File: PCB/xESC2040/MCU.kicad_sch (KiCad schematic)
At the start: 20 parts, among them J6 Conn_01x02, U2 RP2040, U3 W25Q128JVP, Y1 Crystal_GND24

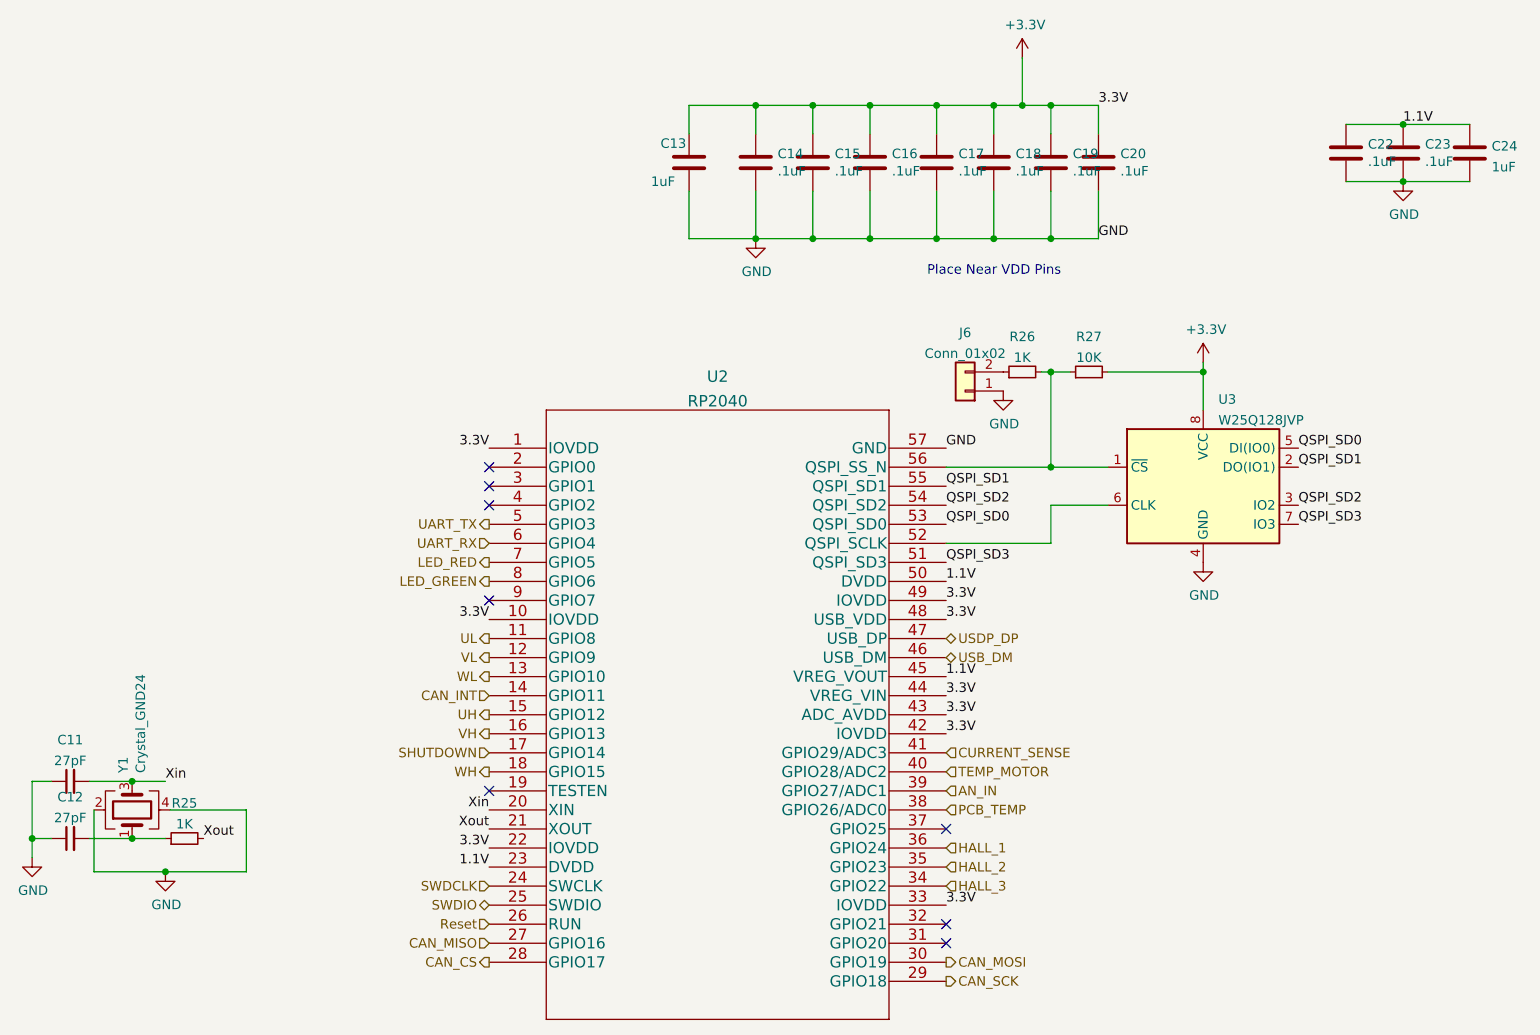
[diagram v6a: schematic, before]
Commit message: Merge J5 and J1 into one connector - no pinout changes or connector move
With J5 gone had kicad redo  reference designators - hope that's ok
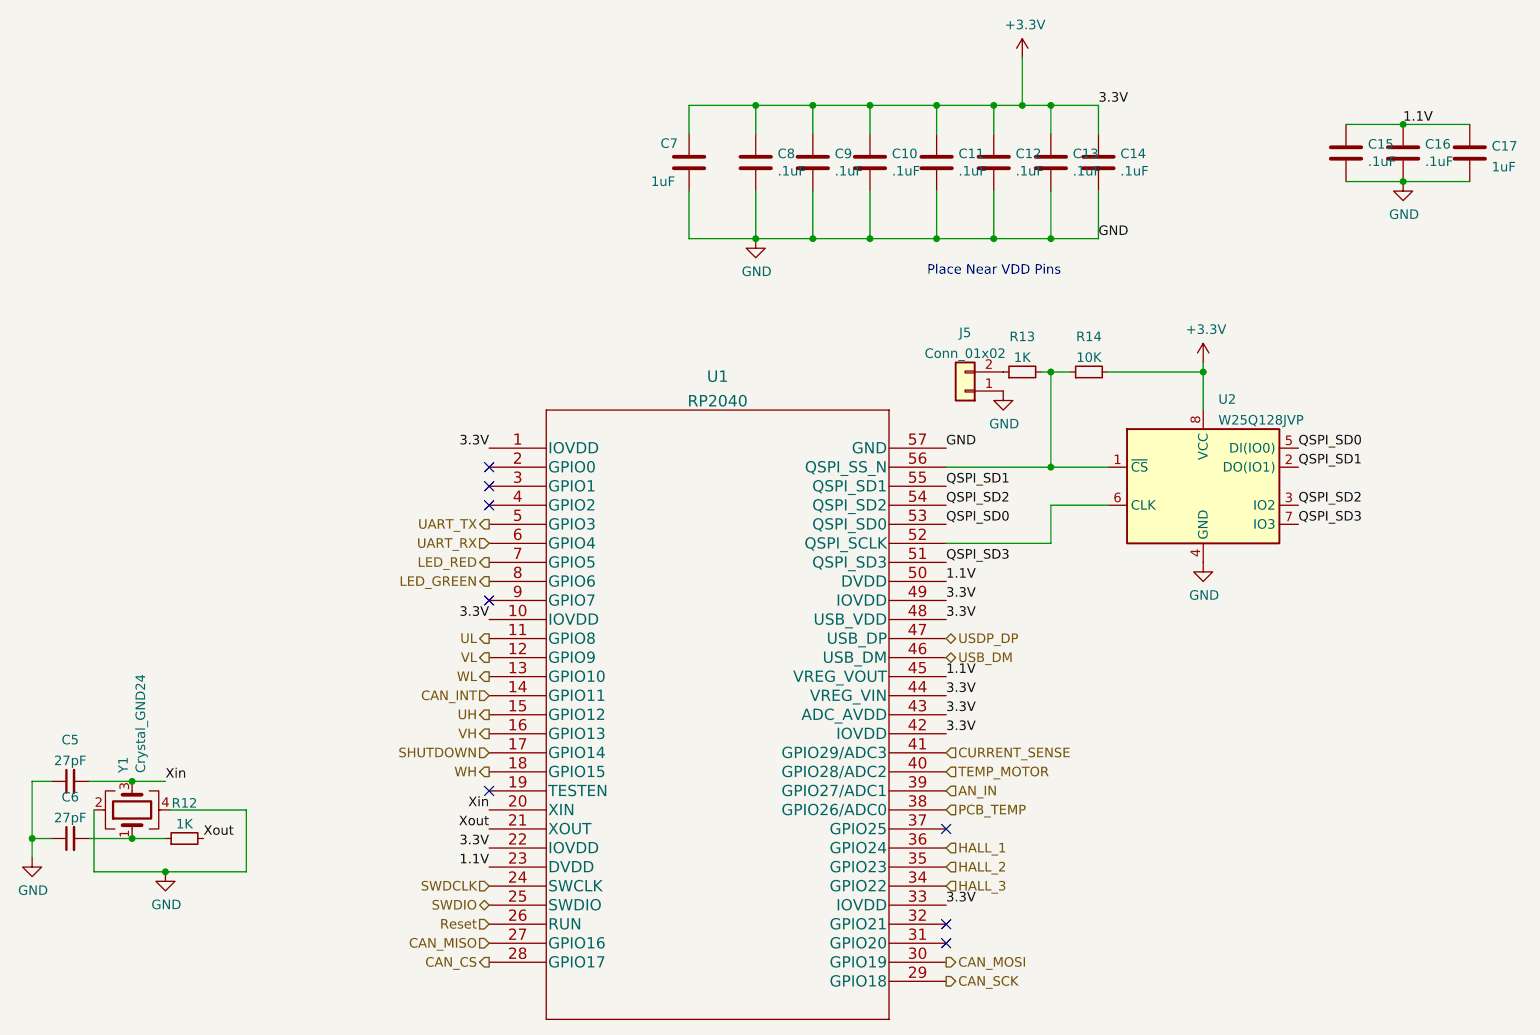
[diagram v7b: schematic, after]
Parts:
- renumbered C16 to C10, C17 to C11, C18 to C12, C19 to C13, C20 to C14, C22 to C15, C23 to C16, C24 to C17, C11 to C5, C12 to C6, C13 to C7, C14 to C8, C15 to C9, J6 to J5, R25 to R12, R26 to R13, R27 to R14, U2 to U1, U3 to U2
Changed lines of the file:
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@@
   (symbol (lib_id "Device:C") (at 170.18 29.21 0) (unit 1)
     (in_bom yes) (on_board yes)
-    (property "Reference" "C17" (id 0) (at 173.101 28.0416 0)
+    (property "Reference" "C11" (id 0) (at 173.101 28.0416 0)
       (effects (font (size 1.27 1.27)) (justify left))
     )
@@
   (symbol (lib_id "Device:C") (at 177.8 29.21 0) (unit 1)
     (in_bom yes) (on_board yes)
-    (property "Reference" "C18" (id 0) (at 180.721 28.0416 0)
+    (property "Reference" "C12" (id 0) (at 180.721 28.0416 0)
       (effects (font (size 1.27 1.27)) (justify left))
     )
@@
   (symbol (lib_id "Device:C") (at 185.42 29.21 0) (unit 1)
     (in_bom yes) (on_board yes)
-    (property "Reference" "C19" (id 0) (at 188.341 28.0416 0)
+    (property "Reference" "C13" (id 0) (at 188.341 28.0416 0)
       (effects (font (size 1.27 1.27)) (justify left))
     )
@@
   (symbol (lib_id "Device:C") (at 191.77 29.21 0) (unit 1)
     (in_bom yes) (on_board yes)
-    (property "Reference" "C20" (id 0) (at 194.691 28.0416 0)
+    (property "Reference" "C14" (id 0) (at 194.691 28.0416 0)
       (effects (font (size 1.27 1.27)) (justify left))
     )
@@
   (symbol (lib_id "power:+3.3V") (at 181.61 15.24 0) (unit 1)
     (in_bom yes) (on_board yes)
-    (property "Reference" "#PWR020" (id 0) (at 181.61 19.05 0)
+    (property "Reference" "#PWR018" (id 0) (at 181.61 19.05 0)
       (effects (font (size 1.27 1.27)) hide)
     )
@@
   (symbol (lib_id "power:GND") (at 146.05 39.37 0) (unit 1)
     (in_bom yes) (on_board yes)
-    (property "Reference" "#PWR018" (id 0) (at 146.05 45.72 0)
+    (property "Reference" "#PWR016" (id 0) (at 146.05 45.72 0)
       (effects (font (size 1.27 1.27)) hide)
     )
@@
   (symbol (lib_id "Device:C") (at 224.79 27.94 0) (unit 1)
     (in_bom yes) (on_board yes)
-    (property "Reference" "C22" (id 0) (at 227.711 26.7716 0)
+    (property "Reference" "C15" (id 0) (at 227.711 26.7716 0)
       (effects (font (size 1.27 1.27)) (justify left))
     )
@@
   (symbol (lib_id "power:GND") (at 232.41 31.75 0) (unit 1)
     (in_bom yes) (on_board yes)
-    (property "Reference" "#PWR024" (id 0) (at 232.41 38.1 0)
+    (property "Reference" "#PWR021" (id 0) (at 232.41 38.1 0)
       (effects (font (size 1.27 1.27)) hide)
     )
@@
   (symbol (lib_id "OpenMower:RP2040") (at 110.49 67.31 0) (unit 1)
     (in_bom yes) (on_board yes) (fields_autoplaced)
-    (property "Reference" "U2" (id 0) (at 140.97 57.7626 0)
+    (property "Reference" "U1" (id 0) (at 140.97 57.7626 0)
       (effects (font (size 1.524 1.524)))
     )
@@
   (symbol (lib_id "Memory_Flash:W25Q128JVS") (at 205.74 72.39 0) (unit 1)
     (in_bom yes) (on_board yes) (fields_autoplaced)
-    (property "Reference" "U3" (id 0) (at 207.7594 60.8035 0)
+    (property "Reference" "U2" (id 0) (at 207.7594 60.8035 0)
       (effects (font (size 1.27 1.27)) (justify left))
     )
@@
   (symbol (lib_id "Device:C") (at 146.05 29.21 0) (unit 1)
     (in_bom yes) (on_board yes)
-    (property "Reference" "C14" (id 0) (at 148.971 28.0416 0)
+    (property "Reference" "C8" (id 0) (at 148.971 28.0416 0)
       (effects (font (size 1.27 1.27)) (justify left))
     )
@@
   (symbol (lib_id "power:GND") (at 67.31 123.825 0) (unit 1)
     (in_bom yes) (on_board yes)
-    (property "Reference" "#PWR0112" (id 0) (at 67.31 130.175 0)
+    (property "Reference" "#PWR015" (id 0) (at 67.31 130.175 0)
       (effects (font (size 1.27 1.27)) hide)
     )
@@
   (symbol (lib_id "power:+3.3V") (at 205.74 55.88 0) (unit 1)
     (in_bom yes) (on_board yes)
-    (property "Reference" "#PWR022" (id 0) (at 205.74 59.69 0)
+    (property "Reference" "#PWR019" (id 0) (at 205.74 59.69 0)
       (effects (font (size 1.27 1.27)) hide)
     )
@@
   (symbol (lib_id "Connector_Generic:Conn_01x02") (at 173.99 59.69 180) (unit 1)
     (in_bom yes) (on_board yes) (fields_autoplaced)
-    (property "Reference" "J6" (id 0) (at 173.99 51.9135 0))
+    (property "Reference" "J5" (id 0) (at 173.99 51.9135 0))
     (property "Value" "Conn_01x02" (id 1) (at 173.99 54.6886 0))
     (property "Footprint" "Connector_PinHeader_2.54mm:PinHeader_1x02_P2.54mm_Vertical" (id 2) (at 173.99 59.69 0)
@@
   (symbol (lib_id "power:GND") (at 205.74 82.55 0) (unit 1)
     (in_bom yes) (on_board yes)
-    (property "Reference" "#PWR023" (id 0) (at 205.74 88.9 0)
+    (property "Reference" "#PWR020" (id 0) (at 205.74 88.9 0)
       (effects (font (size 1.27 1.27)) hide)
     )
@@
   (symbol (lib_id "Device:C") (at 232.41 27.94 0) (unit 1)
     (in_bom yes) (on_board yes)
-    (property "Reference" "C23" (id 0) (at 235.331 26.7716 0)
+    (property "Reference" "C16" (id 0) (at 235.331 26.7716 0)
       (effects (font (size 1.27 1.27)) (justify left))
     )
@@
   (symbol (lib_id "Device:C_Small") (at 54.61 111.76 90) (unit 1)
     (in_bom yes) (on_board yes) (fields_autoplaced)
-    (property "Reference" "C11" (id 0) (at 54.6163 106.2314 90))
+    (property "Reference" "C5" (id 0) (at 54.6163 106.2314 90))
     (property "Value" "27pF" (id 1) (at 54.6163 109.0065 90))
     (property "Footprint" "Capacitor_SMD:C_0603_1608Metric" (id 2) (at 54.61 111.76 0)
@@
   (symbol (lib_id "Device:C") (at 161.29 29.21 0) (unit 1)
     (in_bom yes) (on_board yes)
-    (property "Reference" "C16" (id 0) (at 164.211 28.0416 0)
+    (property "Reference" "C10" (id 0) (at 164.211 28.0416 0)
       (effects (font (size 1.27 1.27)) (justify left))
     )
@@
   (symbol (lib_id "Device:C") (at 241.3 27.94 0) (unit 1)
     (in_bom yes) (on_board yes) (fields_autoplaced)
-    (property "Reference" "C24" (id 0) (at 244.221 27.0315 0)
+    (property "Reference" "C17" (id 0) (at 244.221 27.0315 0)
       (effects (font (size 1.27 1.27)) (justify left))
     )
@@
   (symbol (lib_id "Device:R_Small") (at 181.61 57.15 90) (unit 1)
     (in_bom yes) (on_board yes) (fields_autoplaced)
-    (property "Reference" "R26" (id 0) (at 181.61 52.4469 90))
+    (property "Reference" "R13" (id 0) (at 181.61 52.4469 90))
     (property "Value" "1K" (id 1) (at 181.61 55.222 90))
     (property "Footprint" "Resistor_SMD:R_0603_1608Metric" (id 2) (at 181.61 57.15 0)
@@
   (symbol (lib_id "Device:C") (at 137.16 29.21 0) (unit 1)
     (in_bom yes) (on_board yes)
-    (property "Reference" "C13" (id 0) (at 133.35 26.67 0)
+    (property "Reference" "C7" (id 0) (at 133.35 26.67 0)
       (effects (font (size 1.27 1.27)) (justify left))
     )
@@
   (symbol (lib_id "Device:R_Small") (at 69.85 119.38 90) (unit 1)
     (in_bom yes) (on_board yes) (fields_autoplaced)
-    (property "Reference" "R25" (id 0) (at 69.85 114.6769 90))
+    (property "Reference" "R12" (id 0) (at 69.85 114.6769 90))
     (property "Value" "1K" (id 1) (at 69.85 117.452 90))
     (property "Footprint" "Resistor_SMD:R_0603_1608Metric" (id 2) (at 69.85 119.38 0)
@@
   (symbol (lib_id "power:GND") (at 179.07 59.69 0) (unit 1)
     (in_bom yes) (on_board yes)
-    (property "Reference" "#PWR019" (id 0) (at 179.07 66.04 0)
+    (property "Reference" "#PWR017" (id 0) (at 179.07 66.04 0)
       (effects (font (size 1.27 1.27)) hide)
     )
@@
   (symbol (lib_id "Device:C") (at 153.67 29.21 0) (unit 1)
     (in_bom yes) (on_board yes)
-    (property "Reference" "C15" (id 0) (at 156.591 28.0416 0)
+    (property "Reference" "C9" (id 0) (at 156.591 28.0416 0)
       (effects (font (size 1.27 1.27)) (justify left))
     )
@@
   (symbol (lib_id "power:GND") (at 49.53 121.92 0) (unit 1)
     (in_bom yes) (on_board yes)
-    (property "Reference" "#PWR017" (id 0) (at 49.53 128.27 0)
+    (property "Reference" "#PWR014" (id 0) (at 49.53 128.27 0)
       (effects (font (size 1.27 1.27)) hide)
     )
@@
   (symbol (lib_id "Device:C_Small") (at 54.61 119.38 90) (unit 1)
     (in_bom yes) (on_board yes) (fields_autoplaced)
-    (property "Reference" "C12" (id 0) (at 54.6163 113.8514 90))
+    (property "Reference" "C6" (id 0) (at 54.6163 113.8514 90))
     (property "Value" "27pF" (id 1) (at 54.6163 116.6265 90))
     (property "Footprint" "Capacitor_SMD:C_0603_1608Metric" (id 2) (at 54.61 119.38 0)
@@
   (symbol (lib_id "Device:R_Small") (at 190.5 57.15 90) (unit 1)
     (in_bom yes) (on_board yes) (fields_autoplaced)
-    (property "Reference" "R27" (id 0) (at 190.5 52.4469 90))
+    (property "Reference" "R14" (id 0) (at 190.5 52.4469 90))
     (property "Value" "10K" (id 1) (at 190.5 55.222 90))
     (property "Footprint" "Resistor_SMD:R_0603_1608Metric" (id 2) (at 190.5 57.15 0)

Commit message: BoM data updates
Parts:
- R14: Digikey RC0603FR-0710KL -> 311-10.0KHRCT-ND; Part Number 311-10.0KHRCT-ND -> RC0603FR-0710KL
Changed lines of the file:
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@@
       (effects (font (size 1.27 1.27)) hide)
     )
-    (property "Digikey" "RC0603FR-0710KL" (id 4) (at 190.5 57.15 0)
+    (property "Digikey" "311-10.0KHRCT-ND" (id 4) (at 190.5 57.15 0)
       (effects (font (size 1.27 1.27)) hide)
     )
-    (property "Part Number" "311-10.0KHRCT-ND" (id 5) (at 190.5 57.15 0)
+    (property "Part Number" "RC0603FR-0710KL" (id 5) (at 190.5 57.15 0)
       (effects (font (size 1.27 1.27)) hide)
     )
